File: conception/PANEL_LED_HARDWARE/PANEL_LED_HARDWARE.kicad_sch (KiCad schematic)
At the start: 23 parts, among them J1 PWR, J2 PWR_TO_LED, J3 PWR_TO_LED, J4 Connector to pannel led, J5 EXT PIN, U1 LMR51430, U2 LMR51430, U3 74HC374

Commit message: First version for routage
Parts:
- added C10, C9: 22uF, Capacitor_SMD:C_0603_1608Metric, symbol ESP32-EVB_Rev_H:C
- C1, C11, C2, C4, C5: footprint OLIMEX_RLC-FP:C_0603_5MIL_DWS -> Capacitor_SMD:C_0603_1608Metric
- C3, C6: value 44uF -> 22uF; footprint OLIMEX_RLC-FP:C_0603_5MIL_DWS -> Capacitor_SMD:C_0603_1608Metric
- J5: footprint Connector_PinHeader_1.00mm:PinHeader_1x20_P1.00mm_Vertical -> PANEL_LED:HN1x20
- L1, L2: footprint OLIMEX_RLC-FP:L_0805_5MIL_DWS -> Inductor_SMD:L_Bourns_SRN6045TA
- R1, R3: footprint OLIMEX_RLC-FP:R_0603_5MIL_DWS -> Resistor_SMD:R_0201_0603Metric
- R2, R4: footprint OLIMEX_RLC-FP:R_0603_5MIL_DWS -> Resistor_SMD:R_0402_1005Metric
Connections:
- net +3V3: no longer C11.2, J5.20 (Pin_20)
- net +5V: now also C11.2, J5.20 (Pin_20), C9.1; no longer C3.1
- net +5V Regu 2: now also C10.1; no longer C6.1
- net Vout2: now reaches C5.2, L2.1, U2.2 (SW)
- net FB2: now reaches R3.2, R4.1, U2.4 (FB)
- net CB2: now reaches C5.1, U2.6 (CB)
- net Vout: now reaches C2.2, L1.1, U1.2 (SW)
- net CB: now reaches C2.1, U1.6 (CB)
- net FB: now reaches R1.2, R2.1, U1.4 (FB)
- net GPI016\PANEL_CLK renamed GPI012\PANEL_CLK
- net GPI012\PANEL_CLK: now also J5.7 (Pin_7); no longer J5.11 (Pin_11)
- net GPI032\PANEL_OE renamed GPI04\PANEL_OE
- net GPI04\PANEL_OE: now also J5.6 (Pin_6); no longer J5.13 (Pin_13)
- net GPI05\PANEL_R1 renamed GPI015\PANEL_R1
- net GPI015\PANEL_R1: now also J5.10 (Pin_10); no longer J5.4 (Pin_4)
- net GPIO12\PANEL_B1 renamed GPIO17\PANEL_B1
- net GPIO17\PANEL_B1: now also J5.12 (Pin_12); no longer J5.7 (Pin_7)
- net GPIO14\PANEL_G1 renamed GPIO16\PANEL_G1
- net GPIO16\PANEL_G1: now also J5.11 (Pin_11); no longer J5.9 (Pin_9)
- net GPIO15\PANEL_G2 renamed GPIO32\PANEL_G2
- net GPIO32\PANEL_G2: now also J5.13 (Pin_13); no longer J5.10 (Pin_10)
- net GPIO17\PANEL_R2 renamed GPIO14\PANEL_R2
- net GPIO14\PANEL_R2: now also J5.9 (Pin_9); no longer J5.12 (Pin_12)
- net GPIO4\PANEL_LAT renamed GPIO5\PANEL_LAT
- net GPIO5\PANEL_LAT: now also J5.4 (Pin_4); no longer J5.6 (Pin_6)
- new net: C10.2, C6.1
- new net: C3.1, C9.2
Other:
- moved on the sheet: C3, C6

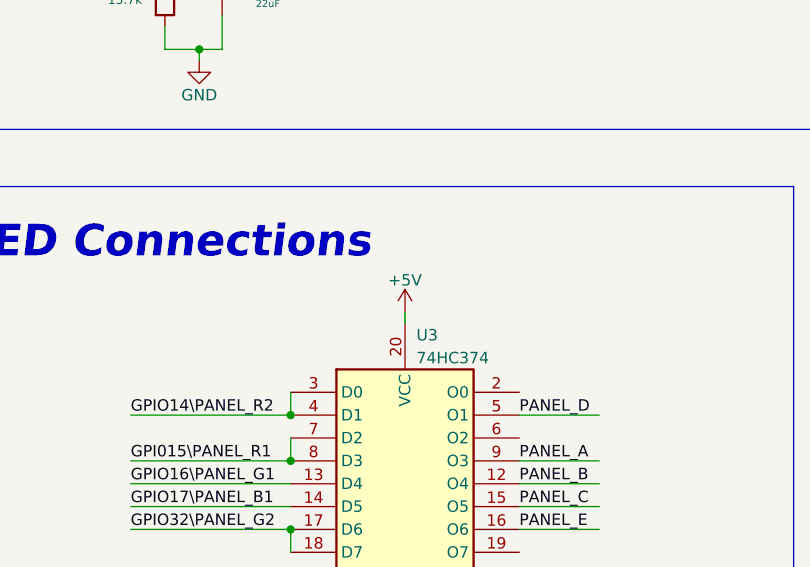
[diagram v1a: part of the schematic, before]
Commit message: Update PCB routage
Increase pistes width for 24V 5V and GND
Change power supply for buffer 5V=>3.3V
Add GND and other signal plan like the example in the datasheet (LMR51430)
Move connectors
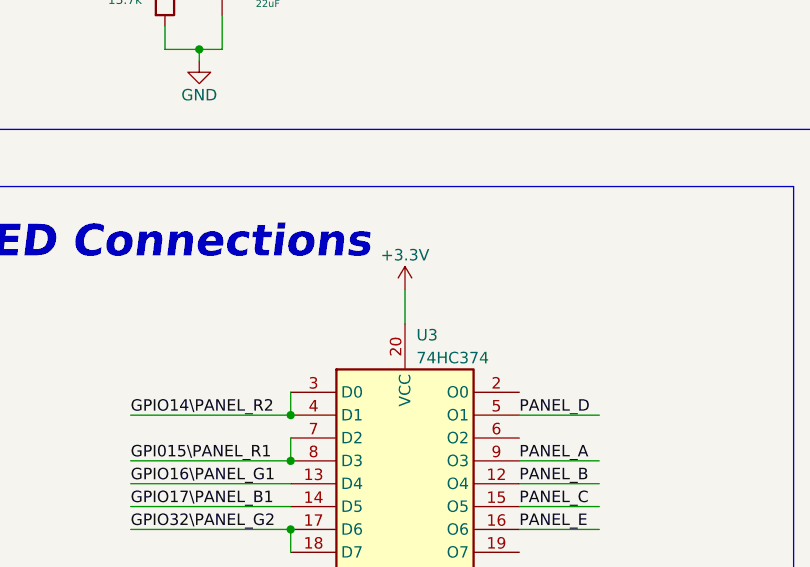
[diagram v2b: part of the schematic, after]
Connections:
- net +3V3: now also U3.20 (VCC)
- net +5V: no longer U3.20 (VCC)
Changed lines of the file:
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@@
+    (stroke (width 0) (type default) (color 0 0 0 0))
+  )
+  (wire (pts (xy 127 137.16) (xy 127 140.97))
     (stroke (width 0) (type default) (color 0 0 0 0))
   )
@@
   )
   (wire (pts (xy 165.1 64.77) (xy 161.29 64.77))
-    (stroke (width 0) (type default) (color 0 0 0 0))
-  )
-  (wire (pts (xy 127 140.97) (xy 127 139.7))
     (stroke (width 0) (type default) (color 0 0 0 0))
   )
@@
     )
     (property "Datasheet" "" (id 3) (at 236.22 41.91 0)
+      (effects (font (size 1.524 1.524)))
+    )
+    (pin "1")
+  )
+  (symbol (lib_id "ESP32-EVB_Rev_H:+3.3V") (at 127 137.16 0) (unit 1)
+    (in_bom yes) (on_board yes)
+    (property "Reference" "#PWR?" (id 0) (at 127 140.97 0)
+      (effects (font (size 1.27 1.27)) hide)
+    )
+    (property "Value" "+3.3V" (id 1) (at 127 133.35 0))
+    (property "Footprint" "" (id 2) (at 127 137.16 0)
+      (effects (font (size 1.524 1.524)))
+    )
+    (property "Datasheet" "" (id 3) (at 127 137.16 0)
       (effects (font (size 1.524 1.524)))
     )
@@
     (pin "2")
   )
-  (symbol (lib_id "ESP32-EVB_Rev_H:+5V") (at 127 139.7 0) (unit 1)
-    (in_bom yes) (on_board yes)
-    (property "Reference" "#PWR0105" (id 0) (at 127 143.51 0)
-      (effects (font (size 1.27 1.27)) hide)
-    )
-    (property "Value" "+5V" (id 1) (at 127 136.144 0))
-    (property "Footprint" "" (id 2) (at 127 139.7 0)
-      (effects (font (size 1.524 1.524)))
-    )
-    (property "Datasheet" "" (id 3) (at 127 139.7 0)
-      (effects (font (size 1.524 1.524)))
-    )
-    (pin "1")
-  )
   (symbol (lib_id "ESP32-EVB_Rev_H:C") (at 53.34 91.44 0) (unit 1)
     (in_bom yes) (on_board yes)
@@
   (symbol (lib_id "ESP32-EVB_Rev_H:GND") (at 172.72 36.83 0) (unit 1)
     (in_bom yes) (on_board yes)
-    (property "Reference" "#PWR?" (id 0) (at 172.72 43.18 0)
+    (property "Reference" "#PWR0115" (id 0) (at 172.72 43.18 0)
       (effects (font (size 1.27 1.27)) hide)
     )
@@
   (symbol (lib_id "power:PWR_FLAG") (at 172.72 33.02 0) (unit 1)
     (in_bom yes) (on_board yes) (fields_autoplaced)
-    (property "Reference" "#FLG?" (id 0) (at 172.72 31.115 0)
+    (property "Reference" "#FLG0101" (id 0) (at 172.72 31.115 0)
       (effects (font (size 1.27 1.27)) hide)
     )
@@
   (symbol_instances
     (path "/de7a83df-dcb9-4bfe-aa9f-88276564bcf2"
-      (reference "#FLG?") (unit 1) (value "PWR_FLAG") (footprint "")
+      (reference "#FLG0101") (unit 1) (value "PWR_FLAG") (footprint "")
     )
     (path "/01eb61d8-64fa-4060-813f-e234fb2636f1"
@@
       (reference "#PWR0104") (unit 1) (value "GND") (footprint "")
     )
-    (path "/36c7b18e-1842-4005-a89c-b35b0df498c2"
-      (reference "#PWR0105") (unit 1) (value "+5V") (footprint "")
-    )
     (path "/c992e090-d727-4990-89c2-1e519c88d6b7"
       (reference "#PWR0106") (unit 1) (value "+5V") (footprint "")
@@
     )
     (path "/5c0b7a0f-1e68-48d4-aa45-7d4cde909c71"
-      (reference "#PWR?") (unit 1) (value "GND") (footprint "")
+      (reference "#PWR0115") (unit 1) (value "GND") (footprint "")
+    )
+    (path "/1a49a86d-39d3-4f05-ad49-ecda7f9b6266"
+      (reference "#PWR?") (unit 1) (value "+3.3V") (footprint "")
     )
     (path "/43a7163f-359f-4007-9c7e-d2d315915827"

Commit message: Review PCB
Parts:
- R2, R4: footprint Resistor_SMD:R_0402_1005Metric -> Resistor_SMD:R_0201_0603Metric
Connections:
- net +5V: now also C6.1
- net +5V Regu 2: now also C3.1
- net GND: now also C10.2, C9.2
- no-connect marks 0 -> 3
